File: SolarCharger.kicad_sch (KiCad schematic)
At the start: 46 parts, among them U2 ADM1176-1ARMZ-R7

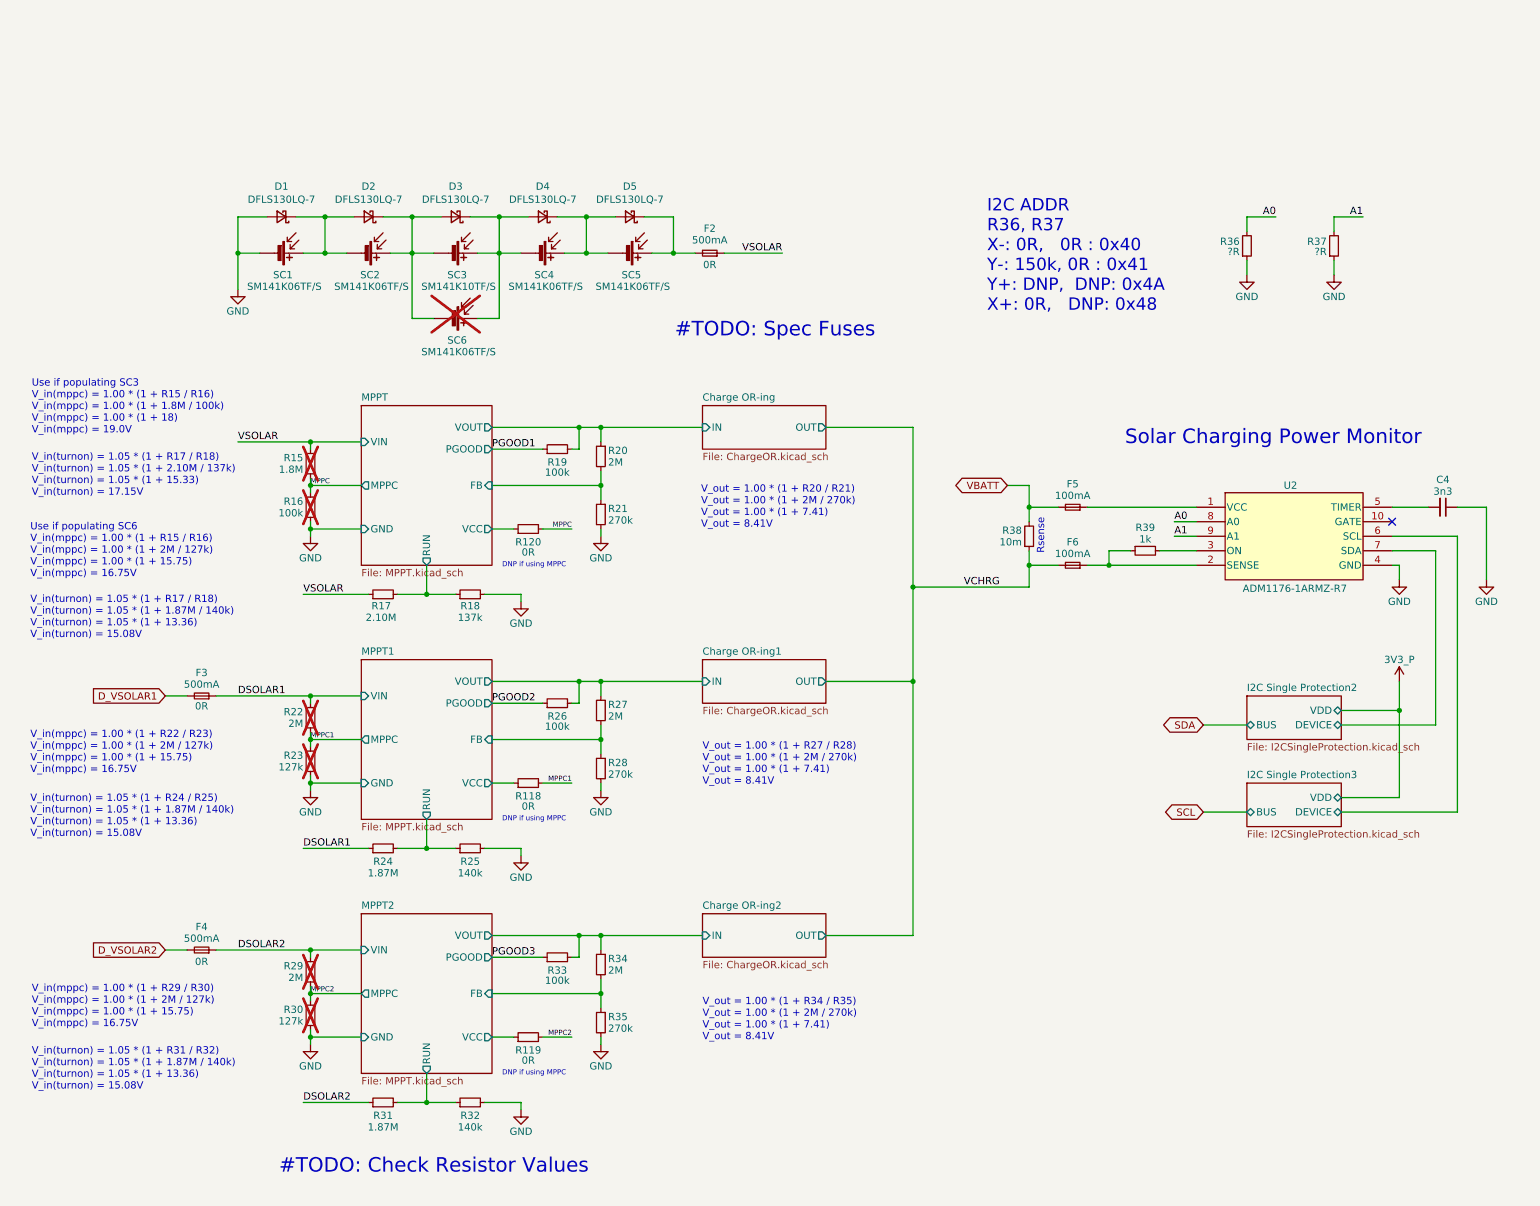
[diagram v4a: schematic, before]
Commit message: V4 Updates and Cell Backer
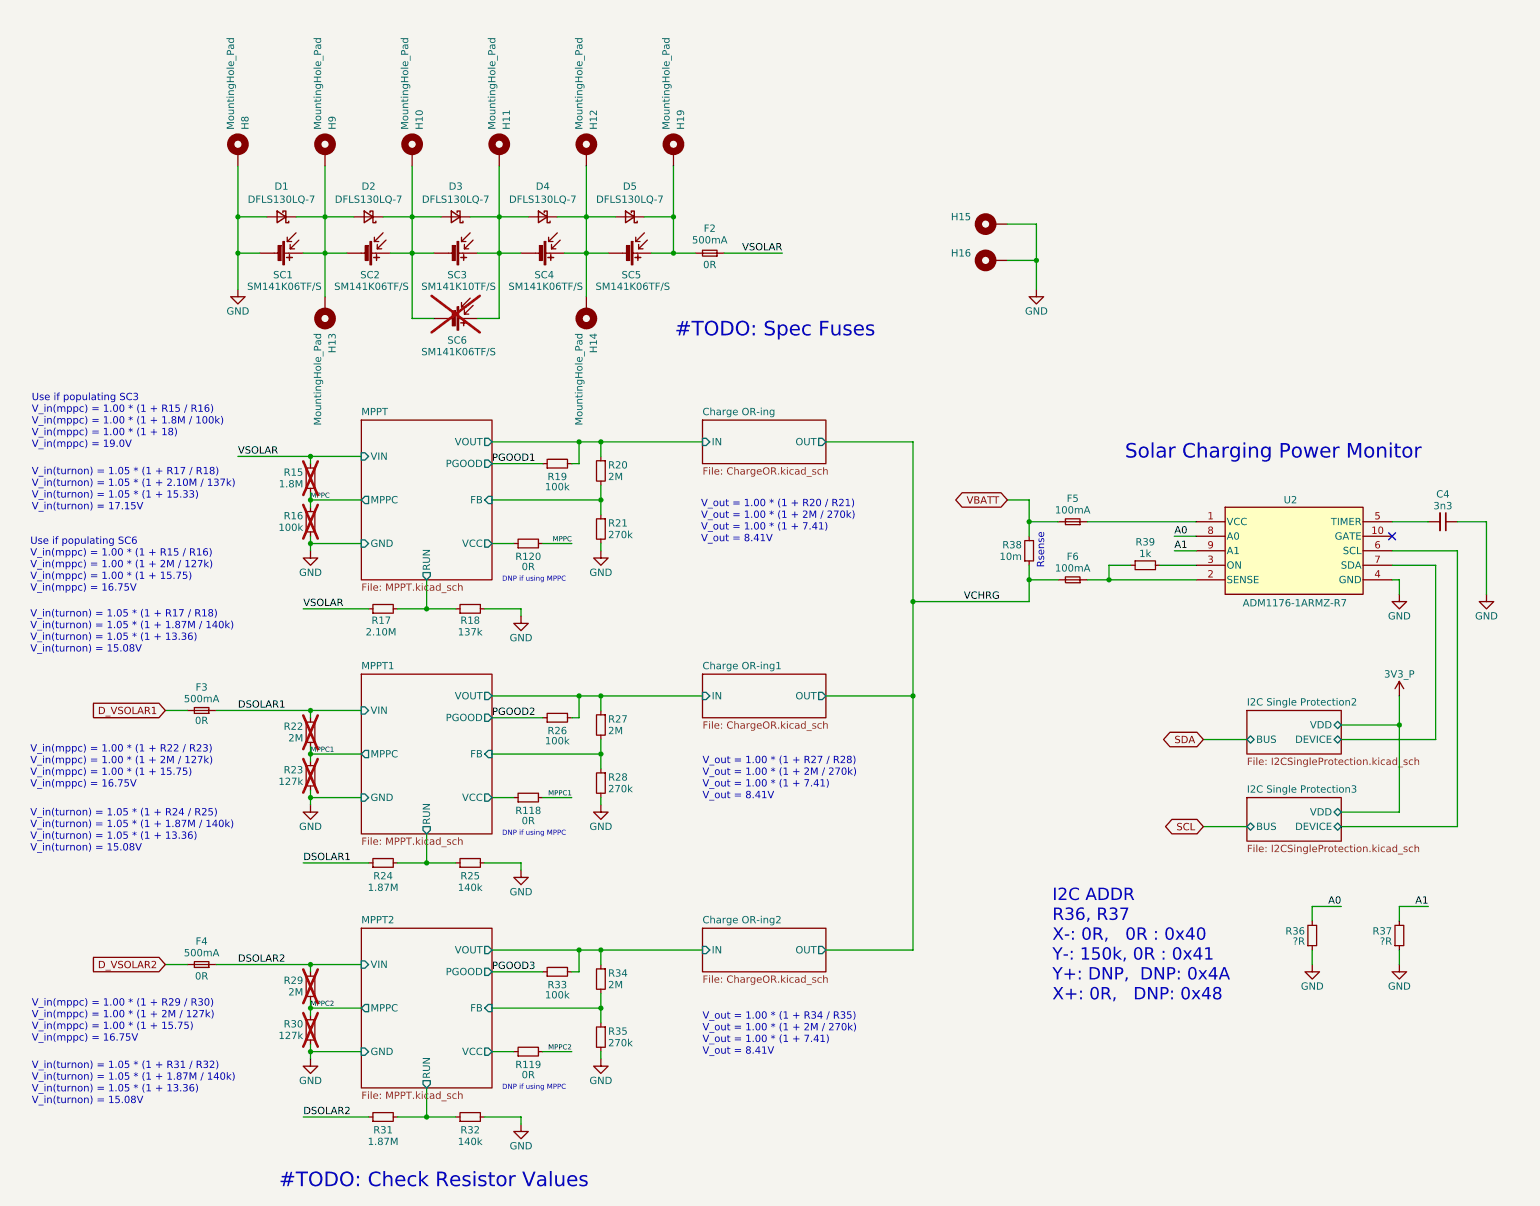
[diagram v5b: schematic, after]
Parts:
- added H10, H11, H12, H13, H14, H15, H16, H19, H8, H9: MountingHole_Pad, TestPoint:TestPoint_Pad_D1.0mm, symbol Mechanical:MountingHole_Pad
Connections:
- net GND: now also H15.1, H16.1, H8.1
- net at D3.1 (K), D4.2 (A), SC3.1 (+)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: now also H11.1
- net at D2.1 (K), D3.2 (A), SC2.1 (+)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: now also H10.1
- net at D4.1 (K), D5.2 (A), SC4.1 (+)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: now also H12.1, H14.1
- net at D1.1 (K), D2.2 (A), SC1.1 (+)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: now also H13.1, H9.1
- net at D5.1 (K), F2.2, SC5.1 (+): now also H19.1
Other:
- moved on the sheet: C4, F3, F4, F5, F6, R118, R119, R120, R15, R16, R17, R18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
